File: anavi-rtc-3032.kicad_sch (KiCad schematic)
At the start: 9 parts, among them J1 Conn_01x06_Pin, U1 RV-3032

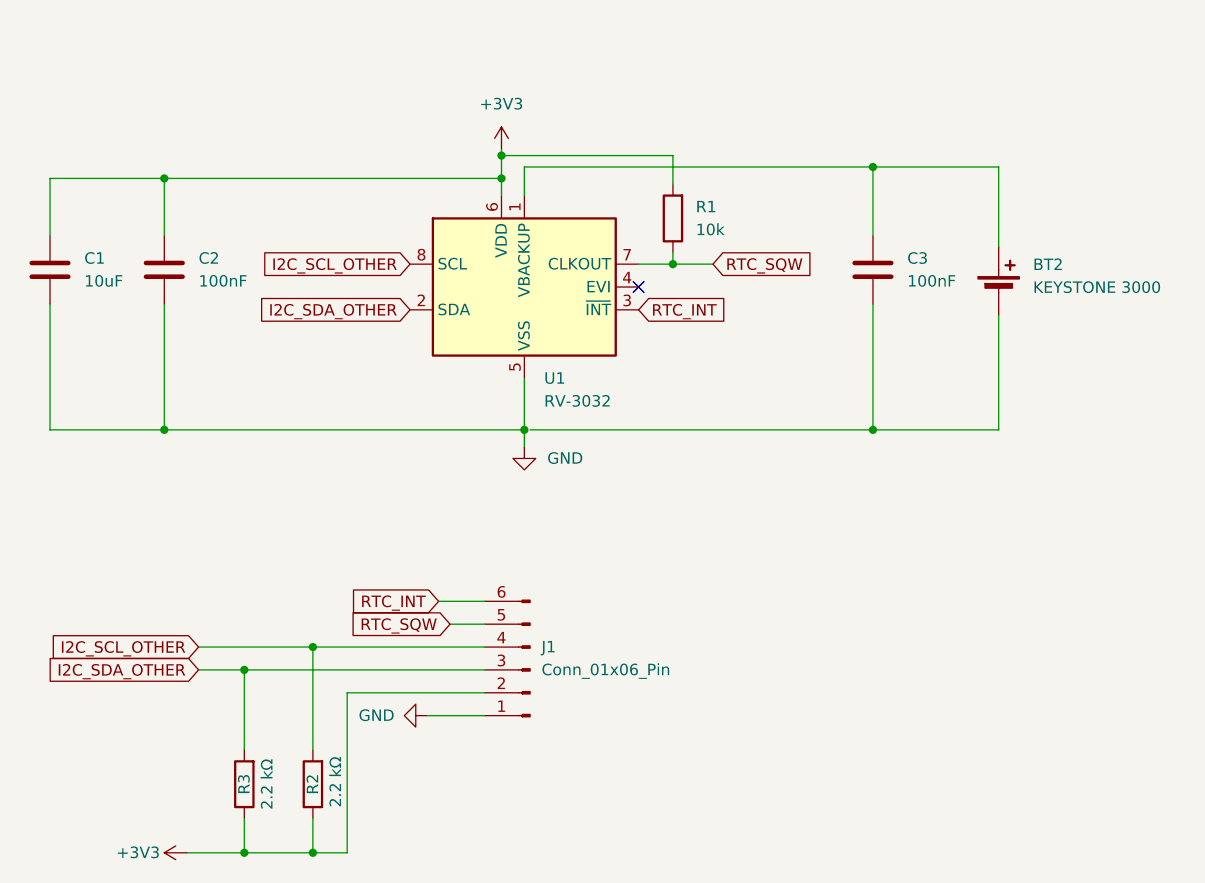
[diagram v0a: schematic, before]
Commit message: Fix ERC issues in schematics
Fix issues in the Electrical Rules Checker (ERC) for the schematics.

Signed-off-by: Leon Anavi <leon@anavi.org>
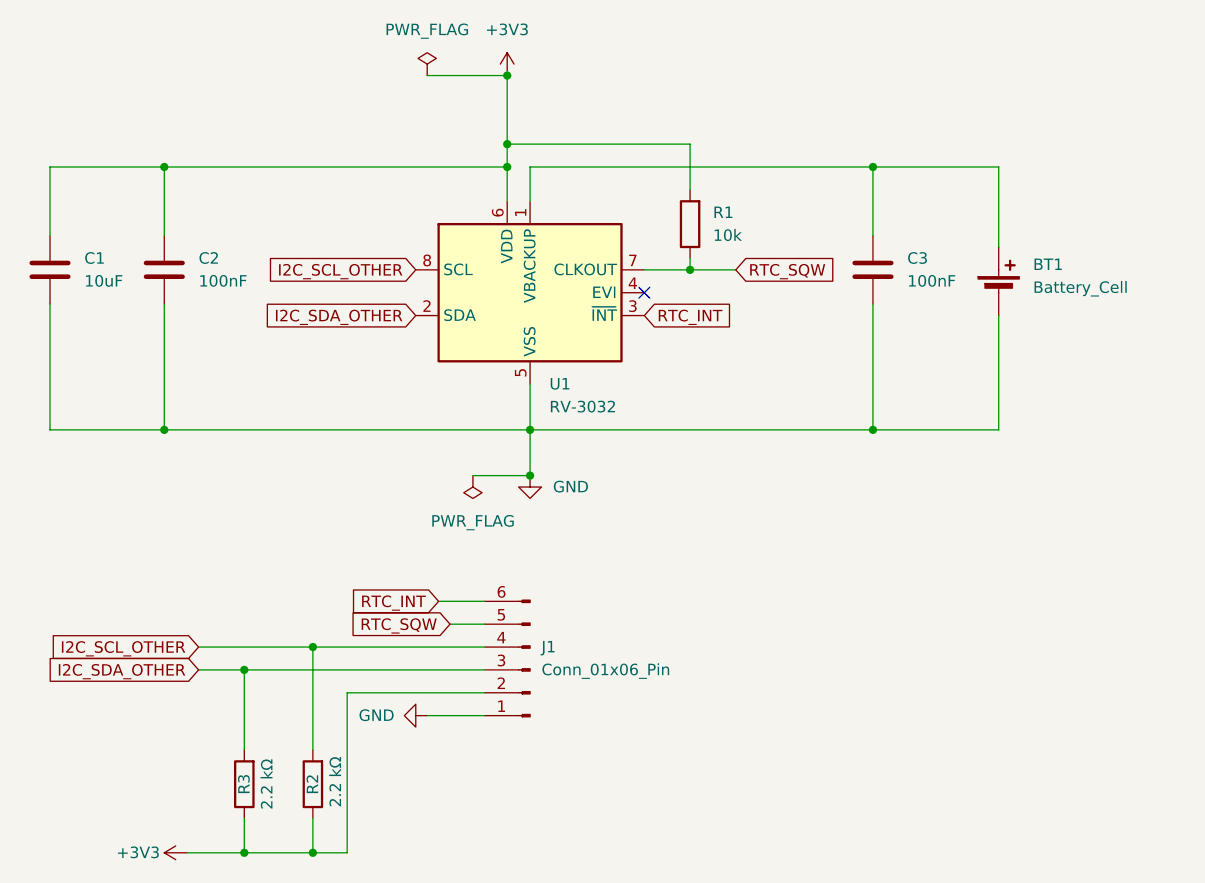
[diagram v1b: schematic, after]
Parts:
- removed BT2: KEYSTONE 3000, Battery:BatteryHolder_Keystone_3000_1x12mm, symbol Device:Battery_Cell
- removed U1: RV-3032, lib:RV-3032, symbol MySymbols:RV-3032
- added BT1: Battery_Cell, Battery:BatteryHolder_Keystone_3000_1x12mm, symbol Device:Battery_Cell
- added U1: RV-3032, lib:RV-3032, symbol rv-3032-c7:RV-3032
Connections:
- net +3V3: now also U1.6 (VDD)
- net GND: now also C3.1, BT1.2 (-), U1.5 (VSS)
- net I2C_SCL_OTHER: now also U1.8 (SCL)
- net I2C_SDA_OTHER: now also U1.2 (SDA)
- net RTC_INT: now also U1.3 (~{INT})
- net RTC_SQW: now also U1.7 (CLKOUT)
- net at C3.2: now also BT1.1 (+), U1.1 (VBACKUP)
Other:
- moved on the sheet: R1

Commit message: Printed Circuit Board
Add the PCB design for hardware revision 1.0.

Signed-off-by: Leon Anavi <leon@anavi.org>
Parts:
- J1: footprint Connector_PinHeader_2.54mm:PinHeader_1x06_P2.54mm_Horizontal -> lib:PinHeader_1x06_P2.54mm_Horizontal-mod
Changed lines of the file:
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@@
 			)
 		)
-		(property "Footprint" "Connector_PinHeader_2.54mm:PinHeader_1x06_P2.54mm_Horizontal"
+		(property "Footprint" "lib:PinHeader_1x06_P2.54mm_Horizontal-mod"
 			(at 96.52 91.44 0)
 			(hide yes)
@@
 	)
 	(symbol
-		(lib_id "Device:Battery_Cell")
-		(at 148.59 49.53 0)
-		(unit 1)
-		(body_style 1)
-		(exclude_from_sim no)
-		(in_bom yes)
-		(on_board yes)
-		(in_pos_files yes)
-		(dnp no)
-		(fields_autoplaced yes)
-		(property "Reference" "BT1"
-			(at 152.4 46.4184 0)
-			(show_name no)
-			(do_not_autoplace no)
-			(effects
-				(font
-					(size 1.27 1.27)
-				)
-				(justify left)
-			)
-		)
-		(property "Value" "Battery_Cell"
-			(at 152.4 48.9584 0)
-			(show_name no)
-			(do_not_autoplace no)
-			(effects
-				(font
-					(size 1.27 1.27)
-				)
-				(justify left)
-			)
-		)
-		(property "Footprint" "Battery:BatteryHolder_Keystone_3000_1x12mm"
-			(at 148.59 48.006 90)
-			(hide yes)
-			(show_name no)
-			(do_not_autoplace no)
-			(effects
-				(font
-					(size 1.27 1.27)
-				)
-			)
-		)
-		(property "Datasheet" ""
-			(at 148.59 48.006 90)
-			(hide yes)
-			(show_name no)
-			(do_not_autoplace no)
-			(effects
-				(font
-					(size 1.27 1.27)
-				)
-			)
-		)
-		(property "Description" "Single-cell battery"
-			(at 148.59 49.53 0)
-			(hide yes)
-			(show_name no)
-			(do_not_autoplace no)
-			(effects
-				(font
-					(size 1.27 1.27)
-				)
-			)
-		)
-		(property "Sim.Device" "V"
-			(at 148.59 49.53 0)
-			(hide yes)
-			(show_name no)
-			(do_not_autoplace no)
-			(effects
-				(font
-					(size 1.27 1.27)
-				)
-			)
-		)
-		(property "Sim.Type" "DC"
-			(at 148.59 49.53 0)
-			(hide yes)
-			(show_name no)
-			(do_not_autoplace no)
-			(effects
-				(font
-					(size 1.27 1.27)
-				)
-			)
-		)
-		(property "Sim.Pins" "1=+ 2=-"
-			(at 148.59 49.53 0)
-			(hide yes)
-			(show_name no)
-			(do_not_autoplace no)
-			(effects
-				(font
-					(size 1.27 1.27)
-				)
-			)
-		)
-		(pin "1"
-		)
-		(pin "2"
-		)
-		(instances
-			(project "anavi-rtc-3032"
-				(path "/3c0e5514-7645-43f4-87ca-051d036b3311"
-					(reference "BT1")
-					(unit 1)
-				)
-			)
-		)
-	)
-	(symbol
 		(lib_id "Device:R")
 		(at 64.77 104.14 180)
@@
 					(unit 1)
 				)
+			)
+		)
+	)
+	(symbol
+		(lib_id "Device:Battery_Cell")
+		(at 148.59 49.53 0)
+		(unit 1)
+		(body_style 1)
+		(exclude_from_sim no)
+		(in_bom yes)
+		(on_board yes)
+		(in_pos_files yes)
+		(dnp no)
+		(fields_autoplaced yes)
+		(property "Reference" "BT1"
+			(at 152.4 46.4184 0)
+			(show_name no)
+			(do_not_autoplace no)
+			(effects
+				(font
+					(size 1.27 1.27)
+				)
+				(justify left)
+			)
+		)
+		(property "Value" "Battery_Cell"
+			(at 152.4 48.9584 0)
+			(show_name no)
+			(do_not_autoplace no)
+			(effects
+				(font
+					(size 1.27 1.27)
+				)
+				(justify left)
+			)
+		)
+		(property "Footprint" "Battery:BatteryHolder_Keystone_3000_1x12mm"
+			(at 148.59 48.006 90)
+			(hide yes)
+			(show_name no)
+			(do_not_autoplace no)
+			(effects
+				(font
+					(size 1.27 1.27)
+				)
+			)
+		)
+		(property "Datasheet" ""
+			(at 148.59 48.006 90)
+			(hide yes)
+			(show_name no)
+			(do_not_autoplace no)
+			(effects
+				(font
+					(size 1.27 1.27)
+				)
+			)
+		)
+		(property "Description" "Single-cell battery"
+			(at 148.59 49.53 0)
+			(hide yes)
+			(show_name no)
+			(do_not_autoplace no)
+			(effects
+				(font
+					(size 1.27 1.27)
+				)
+			)
+		)
+		(property "Sim.Device" "V"
+			(at 148.59 49.53 0)
+			(hide yes)
+			(show_name no)
+			(do_not_autoplace no)
+			(effects
+				(font
+					(size 1.27 1.27)
+				)
+			)
+		)
+		(property "Sim.Type" "DC"
+			(at 148.59 49.53 0)
+			(hide yes)
+			(show_name no)
+			(do_not_autoplace no)
+			(effects
+				(font
+					(size 1.27 1.27)
+				)
+			)
+		)
+		(property "Sim.Pins" "1=+ 2=-"
+			(at 148.59 49.53 0)
+			(hide yes)
+			(show_name no)
+			(do_not_autoplace no)
+			(effects
+				(font
+					(size 1.27 1.27)
+				)
+			)
+		)
+		(pin "2"
+		)
+		(pin "1"
+		)
+		(instances
+			(project "anavi-rtc-3032"
+				(path "/3c0e5514-7645-43f4-87ca-051d036b3311"
+					(reference "BT1")
+					(unit 1)
+				)

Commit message: Add fabrication details
Adjust the PCB layers to add fabrication details.

Signed-off-by: Leon Anavi <leon@anavi.org>
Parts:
- R2, R3: value 2.2 kΩ -> 4.7k
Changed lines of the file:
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@@
 			)
 		)
-		(property "Value" "2.2 kΩ"
+		(property "Value" "4.7k"
 			(at 67.31 104.14 90)
 			(show_name no)
@@
 			)
 		)
-		(property "Value" "2.2 kΩ"
+		(property "Value" "4.7k"
 			(at 74.93 103.886 90)
 			(show_name no)
